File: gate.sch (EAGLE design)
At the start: 42 parts, among them IC1 MAX3232CSE, IC2 LM386M-1, IC3 STM32F072XX, J1 RJ11-2X, X1 MINI-USB-SCHIELD-32005-301

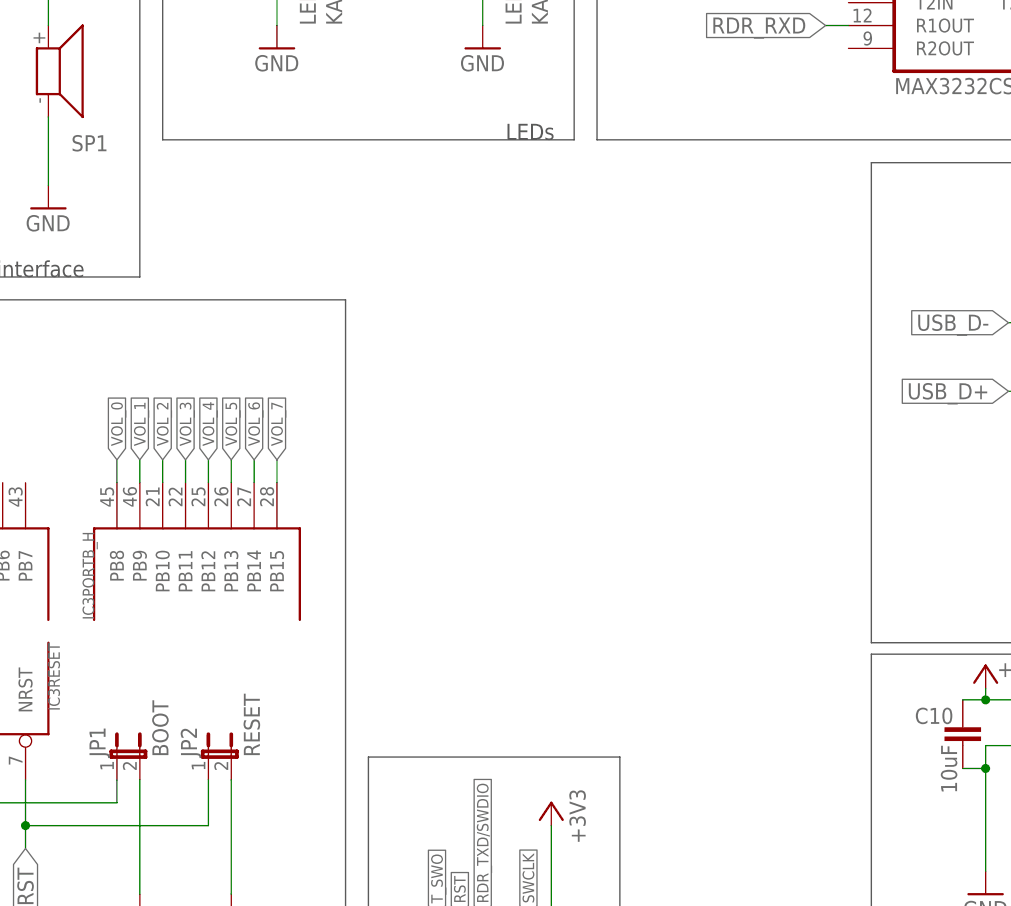
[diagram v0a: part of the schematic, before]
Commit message: Add power supply
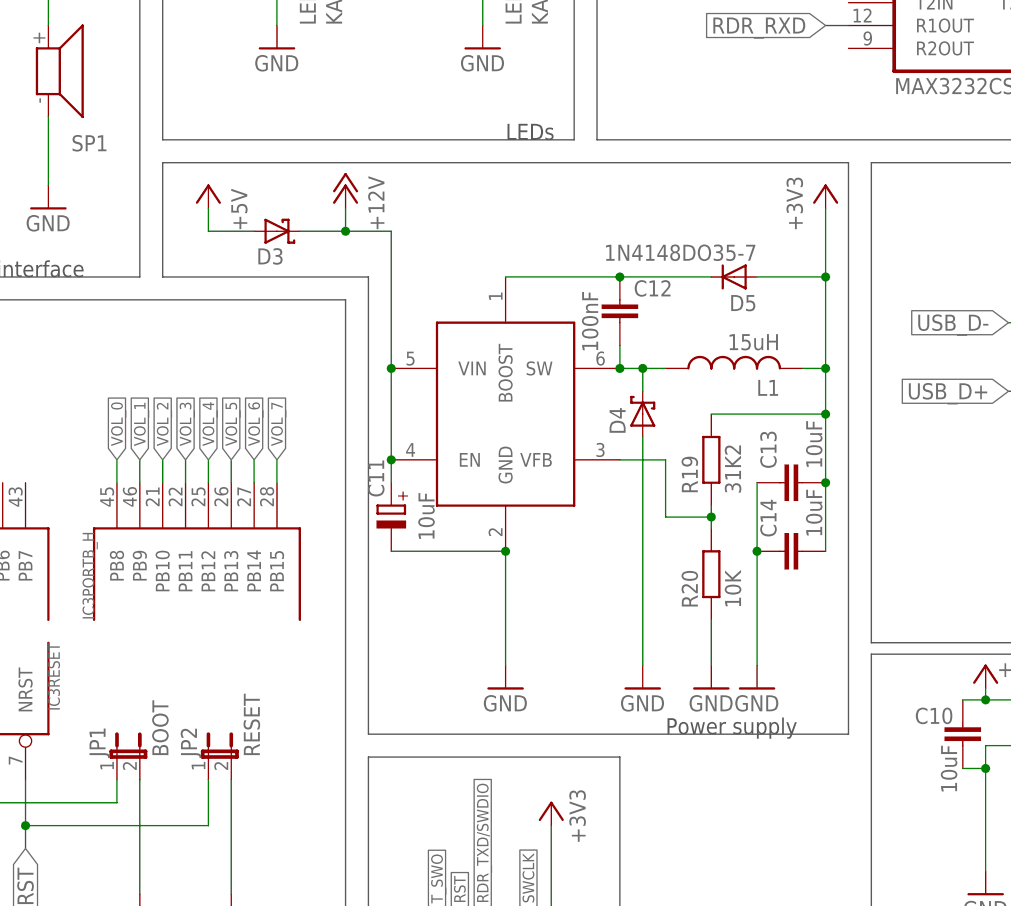
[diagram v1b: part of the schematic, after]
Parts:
- added C11: 10uF, rcl:CPOL-EU153CLV-0505
- added C12: 100nF, rcl:C-EUC0805
- added C13, C14: 10uF, rcl:C-EUC0805
- added D3, D4: (no value), diode:SCHOTTKY-DIODESMD
- added D5: 1N4148DO35-7, diode:1N4148DO35-7
- added L1: 15uH, rcl:L-USPIS2816
- added R19: 31K2, rcl:R-EU_R0805
- added R20: 10K, rcl:R-EU_R0805
- added U$1: MCP16301/H, MCP16301:MCP16301/H
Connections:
- new net N$22: C12.2, D4.C, L1.1, U$1.SW
- new net N$23: C12.1, D5.C, U$1.BOOST
- new net N$25: R19.1, R20.2, U$1.VFB
- net +12V: now also C11.+, D3.C, U$1.EN, U$1.VIN
- net +3V3: now also C13.2, C14.2, D5.A, L1.2, R19.2
- net +5V: now also D3.A
- net GND: now also C11.-, C13.1, C14.1, D4.A, R20.1, U$1.GND
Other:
- note added: "Power supply"
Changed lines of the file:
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@@
 <part name="+3V6" library="supply1" deviceset="+3V3" device=""/>
 <part name="GND16" library="supply1" deviceset="GND" device=""/>
+<part name="U$1" library="MCP16301" deviceset="MCP16301/H" device=""/>
+<part name="P+4" library="supply1" deviceset="+5V" device=""/>
+<part name="P+5" library="supply1" deviceset="+12V" device=""/>
+<part name="D3" library="diode" deviceset="SCHOTTKY-DIODE" device="SMD"/>
+<part name="C11" library="rcl" deviceset="CPOL-EU" device="153CLV-0505" value="10uF"/>
+<part name="GND17" library="supply1" deviceset="GND" device=""/>
+<part name="C12" library="rcl" deviceset="C-EU" device="C0805" value="100nF"/>
+<part name="D4" library="diode" deviceset="SCHOTTKY-DIODE" device="SMD"/>
+<part name="GND18" library="supply1" deviceset="GND" device=""/>
+<part name="L1" library="rcl" deviceset="L-US" device="PIS2816" value="15uH"/>
+<part name="D5" library="diode" deviceset="1N4148" device="DO35-7"/>
+<part name="R19" library="rcl" deviceset="R-EU_" device="R0805" value="31K2"/>
+<part name="R20" library="rcl" deviceset="R-EU_" device="R0805" value="10K"/>
+<part name="GND19" library="supply1" deviceset="GND" device=""/>
+<part name="+3V7" library="supply1" deviceset="+3V3" device=""/>
+<part name="C13" library="rcl" deviceset="C-EU" device="C0805" value="10uF"/>
+<part name="C14" library="rcl" deviceset="C-EU" device="C0805" value="10uF"/>
+<part name="GND20" library="supply1" deviceset="GND" device=""/>
 </parts>
 <sheets>
@@
 <wire x1="129.54" y1="10.16" x2="129.54" y2="45.72" width="0.1524" layer="97"/>
 <text x="152.4" y="10.16" size="1.778" layer="97">SWD</text>
+<wire x1="106.68" y1="111.76" x2="182.88" y2="111.76" width="0.1524" layer="97"/>
+<wire x1="182.88" y1="111.76" x2="182.88" y2="48.26" width="0.1524" layer="97"/>
+<wire x1="182.88" y1="48.26" x2="129.54" y2="48.26" width="0.1524" layer="97"/>
+<wire x1="129.54" y1="48.26" x2="129.54" y2="99.06" width="0.1524" layer="97"/>
+<wire x1="129.54" y1="99.06" x2="106.68" y2="99.06" width="0.1524" layer="97"/>
+<wire x1="106.68" y1="99.06" x2="106.68" y2="111.76" width="0.1524" layer="97"/>
+<text x="162.56" y="48.26" size="1.778" layer="97">Power supply</text>
 </plain>
 <instances>
@@
 </instance>
 <instance part="GND16" gate="1" x="144.78" y="15.24"/>
+<instance part="U$1" gate="G$1" x="144.78" y="83.82"/>
+<instance part="P+4" gate="1" x="111.76" y="109.22" rot="MR0"/>
+<instance part="P+5" gate="1" x="127" y="109.22" rot="MR0"/>
+<instance part="D3" gate="G$1" x="119.38" y="104.14" rot="MR180"/>
+<instance part="C11" gate="G$1" x="132.08" y="73.66" smashed="yes" rot="MR0">
+<attribute name="NAME" x="129.5146" y="74.549" size="1.778" layer="95" rot="MR90"/>
+<attribute name="VALUE" x="135.1026" y="69.723" size="1.778" layer="96" rot="MR90"/>
+</instance>
+<instance part="GND17" gate="1" x="144.78" y="53.34"/>
+<instance part="C12" gate="G$1" x="157.48" y="96.52" smashed="yes">
+<attribute name="NAME" x="159.004" y="96.901" size="1.778" layer="95"/>
+<attribute name="VALUE" x="155.067" y="90.678" size="1.778" layer="96" rot="R90"/>
+</instance>
+<instance part="D4" gate="G$1" x="160.02" y="83.82" rot="R90"/>
+<instance part="GND18" gate="1" x="160.02" y="53.34"/>
+<instance part="L1" gate="G$1" x="170.18" y="88.9" rot="R90"/>
+<instance part="D5" gate="G$1" x="170.18" y="99.06" smashed="yes" rot="R180">
+<attribute name="NAME" x="172.72" y="97.0534" size="1.778" layer="95" rot="R180"/>
+<attribute name="VALUE" x="172.72" y="102.6414" size="1.778" layer="96" rot="R180"/>
+</instance>
+<instance part="R19" gate="G$1" x="167.64" y="78.74" rot="R90"/>
+<instance part="R20" gate="G$1" x="167.64" y="66.04" rot="R90"/>
+<instance part="GND19" gate="1" x="167.64" y="53.34"/>
+<instance part="+3V7" gate="G$1" x="180.34" y="109.22"/>
+<instance part="C13" gate="G$1" x="175.26" y="76.2" rot="R90"/>
+<instance part="C14" gate="G$1" x="175.26" y="68.58" rot="R90"/>
+<instance part="GND20" gate="1" x="172.72" y="53.34"/>
 </instances>
 <busses>
@@
 <wire x1="144.78" y1="22.86" x2="144.78" y2="17.78" width="0.1524" layer="91"/>
 </segment>
+<segment>
+<pinref part="C11" gate="G$1" pin="-"/>
+<pinref part="U$1" gate="G$1" pin="GND"/>
+<wire x1="132.08" y1="68.58" x2="144.78" y2="68.58" width="0.1524" layer="91"/>
+<pinref part="GND17" gate="1" pin="GND"/>
+<wire x1="144.78" y1="68.58" x2="144.78" y2="55.88" width="0.1524" layer="91"/>
+<junction x="144.78" y="68.58"/>
+</segment>
+<segment>
+<pinref part="D4" gate="G$1" pin="A"/>
+<pinref part="GND18" gate="1" pin="GND"/>
+<wire x1="160.02" y1="81.28" x2="160.02" y2="55.88" width="0.1524" layer="91"/>
+</segment>
+<segment>
+<pinref part="R20" gate="G$1" pin="1"/>
+<pinref part="GND19" gate="1" pin="GND"/>
+<wire x1="167.64" y1="60.96" x2="167.64" y2="55.88" width="0.1524" layer="91"/>
+</segment>
+<segment>
+<pinref part="C13" gate="G$1" pin="1"/>
+<pinref part="C14" gate="G$1" pin="1"/>
+<wire x1="172.72" y1="76.2" x2="172.72" y2="68.58" width="0.1524" layer="91"/>
+<pinref part="GND20" gate="1" pin="GND"/>
+<wire x1="172.72" y1="68.58" x2="172.72" y2="55.88" width="0.1524" layer="91"/>
+<junction x="172.72" y="68.58"/>
+</segment>
 </net>
 <net name="N$1" class="0">
@@
 <wire x1="149.86" y1="38.1" x2="149.86" y2="22.86" width="0.1524" layer="91"/>
 </segment>
+<segment>
+<pinref part="D5" gate="G$1" pin="A"/>
+<wire x1="180.34" y1="99.06" x2="172.72" y2="99.06" width="0.1524" layer="91"/>
+<wire x1="180.34" y1="99.06" x2="180.34" y2="106.68" width="0.1524" layer="91"/>
+<pinref part="+3V7" gate="G$1" pin="+3V3"/>
+<pinref part="R19" gate="G$1" pin="2"/>
+<wire x1="167.64" y1="83.82" x2="180.34" y2="83.82" width="0.1524" layer="91"/>
+<wire x1="180.34" y1="99.06" x2="180.34" y2="88.9" width="0.1524" layer="91"/>
+<junction x="180.34" y="99.06"/>
+<pinref part="L1" gate="G$1" pin="2"/>
+<wire x1="180.34" y1="88.9" x2="180.34" y2="83.82" width="0.1524" layer="91"/>
+<wire x1="177.8" y1="88.9" x2="180.34" y2="88.9" width="0.1524" layer="91"/>
+<junction x="180.34" y="88.9"/>
+<pinref part="C13" gate="G$1" pin="2"/>
+<wire x1="180.34" y1="83.82" x2="180.34" y2="76.2" width="0.1524" layer="91"/>
+<junction x="180.34" y="83.82"/>
+<pinref part="C14" gate="G$1" pin="2"/>
+<wire x1="180.34" y1="76.2" x2="180.34" y2="68.58" width="0.1524" layer="91"/>
+<junction x="180.34" y="76.2"/>
+</segment>
 </net>
 <net name="N$3" class="0">
@@
 <pinref part="IC2" gate="G$1" pin="VS"/>
 <wire x1="58.42" y1="147.32" x2="58.42" y2="142.24" width="0.1524" layer="91"/>
+</segment>
+<segment>
+<pinref part="P+4" gate="1" pin="+5V"/>
+<wire x1="111.76" y1="104.14" x2="111.76" y2="106.68" width="0.1524" layer="91"/>
+<pinref part="D3" gate="G$1" pin="A"/>
+<wire x1="116.84" y1="104.14" x2="111.76" y2="104.14" width="0.1524" layer="91"/>
 </segment>
 </net>
@@
 <pinref part="P+1" gate="1" pin="+12V"/>
 </segment>
+<segment>
+<pinref part="D3" gate="G$1" pin="C"/>
+<pinref part="P+5" gate="1" pin="+12V"/>
+<wire x1="127" y1="106.68" x2="127" y2="104.14" width="0.1524" layer="91"/>
+<wire x1="127" y1="104.14" x2="121.92" y2="104.14" width="0.1524" layer="91"/>
+<pinref part="U$1" gate="G$1" pin="VIN"/>
+<wire x1="132.08" y1="88.9" x2="132.08" y2="78.74" width="0.1524" layer="91"/>
+<pinref part="U$1" gate="G$1" pin="EN"/>
+<pinref part="C11" gate="G$1" pin="+"/>
+<wire x1="132.08" y1="78.74" x2="132.08" y2="76.2" width="0.1524" layer="91"/>
+<junction x="132.08" y="78.74"/>
+<junction x="132.08" y="88.9"/>
+<wire x1="127" y1="104.14" x2="132.08" y2="104.14" width="0.1524" layer="91"/>
+<wire x1="132.08" y1="104.14" x2="132.08" y2="88.9" width="0.1524" layer="91"/>
+<junction x="127" y="104.14"/>
+</segment>
 </net>
 <net name="N$19" class="0">
@@
 </segment>
 </net>
+<net name="N$22" class="0">
+<segment>
+<pinref part="U$1" gate="G$1" pin="SW"/>
+<pinref part="C12" gate="G$1" pin="2"/>
+<wire x1="157.48" y1="88.9" x2="157.48" y2="91.44" width="0.1524" layer="91"/>
+<pinref part="D4" gate="G$1" pin="C"/>
+<wire x1="157.48" y1="88.9" x2="160.02" y2="88.9" width="0.1524" layer="91"/>
+<wire x1="160.02" y1="88.9" x2="160.02" y2="86.36" width="0.1524" layer="91"/>
+<junction x="157.48" y="88.9"/>
+<pinref part="L1" gate="G$1" pin="1"/>
+<wire x1="162.56" y1="88.9" x2="160.02" y2="88.9" width="0.1524" layer="91"/>
+<junction x="160.02" y="88.9"/>
+</segment>
+</net>
+<net name="N$23" class="0">
+<segment>
+<pinref part="C12" gate="G$1" pin="1"/>
+<pinref part="U$1" gate="G$1" pin="BOOST"/>
+<wire x1="157.48" y1="99.06" x2="144.78" y2="99.06" width="0.1524" layer="91"/>
+<pinref part="D5" gate="G$1" pin="C"/>
+<wire x1="167.64" y1="99.06" x2="157.48" y2="99.06" width="0.1524" layer="91"/>
+<junction x="157.48" y="99.06"/>
+</segment>
+</net>
+<net name="N$25" class="0">
+<segment>
+<pinref part="R19" gate="G$1" pin="1"/>
+<pinref part="R20" gate="G$1" pin="2"/>
+<wire x1="167.64" y1="73.66" x2="167.64" y2="72.39" width="0.1524" layer="91"/>
+<wire x1="167.64" y1="72.39" x2="167.64" y2="71.12" width="0.1524" layer="91"/>
+<wire x1="167.64" y1="72.39" x2="162.56" y2="72.39" width="0.1524" layer="91"/>
+<wire x1="162.56" y1="72.39" x2="162.56" y2="78.74" width="0.1524" layer="91"/>
+<junction x="167.64" y="72.39"/>
+<pinref part="U$1" gate="G$1" pin="VFB"/>
+<wire x1="162.56" y1="78.74" x2="157.48" y2="78.74" width="0.1524" layer="91"/>
+</segment>
+</net>

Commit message: Finishing touches for revA
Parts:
- removed U$1: MCP16301/H, MCP16301:MCP16301/H
- added IC4: MAX3232CSE, maxim:MAX3232CSE
- added R21: 100K, rcl:R-EU_R0805
- C1, C2, C3: value (none) -> 10uF; device rcl:CPOL-EU153CLV-0505 -> rcl:C-EUC0805
- C10, C13, C14: value 10uF -> (none); device rcl:C-EUC0805 -> rcl:CPOL-EU153CLV-0505
- C11: value 10uF -> (none)
- C12: value 100nF -> 10uF
- C4: value (none) -> 50nF; device rcl:CPOL-EU153CLV-0505 -> rcl:C-EUC0805
- C5: value 50nF -> 250uF
- C6: value 250uF -> 10uF; device rcl:C-EUC0805 -> rcl:CPOL-EU153CLV-0505
- C7: value 10uF -> 100nF
- D3: value (none) -> 1N4148DO35-7; device diode:SCHOTTKY-DIODESMD -> diode:1N4148DO35-7
- D5: value 1N4148DO35-7 -> (none); device diode:1N4148DO35-7 -> diode:SCHOTTKY-DIODESMD
- IC1: value MAX3232CSE -> LM386M-1; device maxim:MAX3232CSE -> linear:LM386M-1
- IC2: value LM386M-1 -> STM32F072XX; device linear:LM386M-1 -> stm32f051:STM32F072XX
- IC3: value STM32F072XX -> MCP16301/H; device stm32f051:STM32F072XX -> MCP16301:MCP16301/H
- R1, R2: value 22R -> TODO
- R10, R7, R8, R9: value 330R -> TODO
- R11: value TODO -> 10R
- R12, R13, R14, R15: value TODO -> 330R
- R16: value TODO -> 31K2
- R17: value TODO -> 10K
- R18: value TODO -> 22R
- R19: value 31K2 -> 22R
- R20: value 10K -> 1K5
- R3: value 100K -> TODO
- R4: value 1K5 -> TODO
- R6: value 10R -> TODO
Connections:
- net +12V: now also C6.+, D5.C, IC3.EN, IC3.VIN; no longer C11.+, D3.C, U$1.EN, U$1.VIN
- net +3V3: now also C1.1, C12.1, C13.-, C2.1, C3.1, C8.2, C9.2, D3.A, IC2AN_POWER.VBAT, IC2AN_POWER.VDDA, IC2POWER.VDD_1, IC2POWER.VDD_2, IC2POWER.VDD_3, IC4P.VCC, R16.2, R20.1; no longer C1.-, C10.1, C13.2, C14.2, C7.1, C8.1, C9.1, D5.A, IC1P.VCC, IC3AN_POWER.VBAT, IC3AN_POWER.VDDA, IC3POWER.VDD_1, IC3POWER.VDD_2, IC3POWER.VDD_3, R19.2, R4.1
- net +5V: now also D1.A, D4.C, IC1.VS; no longer D2.C, D3.A, IC2.VS
- net AUDIO_OUT: now also IC2PORTA_L.PA4, R10.2; no longer IC3PORTA_L.PA4, R5.2
- net BOOT0: now also IC2RESET.BOOT0; no longer IC3RESET.BOOT0
- net GND: now also C1.2, C12.2, C14.+, C2.2, C3.2, C6.-, C8.1, C9.1, D2.A, IC1.-IN, IC1.GND, IC2AN_POWER.VSSA, IC2POWER.VSS_1, IC2POWER.VSS_2, IC2POWER.VSS_3, IC3.GND, IC4P.GND, R11.1, R17.1, R21.1, R9.1; no longer C10.2, C11.-, C13.1, C14.1, C2.+, C7.2, C8.2, C9.2, D4.A, IC1P.GND, IC2.-IN, IC2.GND, IC3AN_POWER.VSSA, IC3POWER.VSS_1, IC3POWER.VSS_2, IC3POWER.VSS_3, R20.1, R3.1, R6.1, U$1.GND
- net LED_G1: now also IC2PORTB_L.PB1, R13.2; no longer IC3PORTB_L.PB1, R8.2
- net LED_G2: now also IC2PORTA_H.PA8, R15.2; no longer IC3PORTA_H.PA8, R10.2
- net LED_R1: now also IC2PORTB_L.PB0, R12.2; no longer IC3PORTB_L.PB0, R7.2
- net LED_R2: now also IC2PORTA_H.PA9, R14.2; no longer IC3PORTA_H.PA9, R9.2
- net N$1: now also IC4G$1.R1IN; no longer IC1G$1.R1IN
- net N$10: now also R14.1; no longer R9.1
- net N$11: now also D4.A; no longer D2.A
- net N$12: now also R18.2; no longer R1.2
- net N$13: now also R19.2, R20.2; no longer R2.2, R4.2
- net N$14: now also R21.2; no longer R3.2
- net N$15: now also IC1.+IN, R1.2, R10.1, R2.2, R3.2, R4.2, R5.2, R6.2, R7.2, R8.2, R9.2; no longer IC2.+IN, R11.2, R12.2, R13.2, R14.2, R15.2, R16.2, R17.2, R18.2, R5.1
- net N$16: now also C4.1, IC1.OUT; no longer C6.1, IC2.OUT
- net N$17: now also C4.2, R11.2; no longer C5.2, R6.2
- net N$18: now also C5.2; no longer C6.2
- net N$19: now also R12.1; no longer R7.1
- net N$2: now also IC4G$1.T1OUT; no longer IC1G$1.T1OUT
- net N$20: now also R13.1; no longer R8.1
- net N$21: now also R15.1; no longer R10.1
- net N$22: now also C7.2, D2.C, IC3.SW; no longer C12.2, D4.C, U$1.SW
- net N$23: now also C7.1, D3.C, IC3.BOOST; no longer C12.1, D5.C, U$1.BOOST
- net N$25: now also IC3.VFB, R16.1, R17.2; no longer R19.1, R20.2, U$1.VFB
- net N$3: now also C10.+, IC4G$1.C1+; no longer C3.+, IC1G$1.C1+
- net N$4: now also C10.-, IC4G$1.C1-; no longer C3.-, IC1G$1.C1-
- net N$5: now also C11.+, IC4G$1.C2+; no longer C4.+, IC1G$1.C2+
- net N$6: now also C11.-, IC4G$1.C2-; no longer C4.-, IC1G$1.C2-
- net N$7: now also C13.+, IC4G$1.V+; no longer C1.+, IC1G$1.V+
- net N$8: now also C14.-, IC4G$1.V-; no longer C2.-, IC1G$1.V-
- net N$9: now also D5.A; no longer D1.A
- net RDR_RXD: now also IC2PORTA_H.PA15, IC4G$1.R1OUT; no longer IC1G$1.R1OUT, IC3PORTA_H.PA15
- net RDR_TXD/SWDIO: now also IC2PORTA_H.PA14, IC4G$1.T1IN; no longer IC1G$1.T1IN, IC3PORTA_H.PA14
- net RFID_IRQ: now also IC2PORTA_L.PA0; no longer IC3PORTA_L.PA0
- net RFID_MISO: now also IC2PORTA_L.PA6; no longer IC3PORTA_L.PA6
- net RFID_MOSI: now also IC2PORTA_L.PA7; no longer IC3PORTA_L.PA7
- net RFID_RST: now also IC2PORTA_L.PA3; no longer IC3PORTA_L.PA3
- net RFID_SCK: now also IC2PORTA_L.PA5; no longer IC3PORTA_L.PA5
- net RFID_SS: now also IC2PORTA_L.PA1; no longer IC3PORTA_L.PA1
- net RST: now also IC2RESET.NRST; no longer IC3RESET.NRST
- net SWCLK: now also IC2PORTA_H.PA13; no longer IC3PORTA_H.PA13
- net T_SWO: now also IC2PORTB_L.PB3; no longer IC3PORTB_L.PB3
- net USB_D+: now also IC2PORTA_H.PA11, R19.1; no longer IC3PORTA_H.PA11, R2.1
- net USB_D-: now also IC2PORTA_H.PA12, R18.1; no longer IC3PORTA_H.PA12, R1.1
- net VOL_0: now also IC2PORTB_H.PB8, R1.1; no longer IC3PORTB_H.PB8, R11.1
- net VOL_1: now also IC2PORTB_H.PB9, R2.1; no longer IC3PORTB_H.PB9, R12.1
- net VOL_2: now also IC2PORTB_H.PB10, R3.1; no longer IC3PORTB_H.PB10, R13.1
- net VOL_3: now also IC2PORTB_H.PB11, R4.1; no longer IC3PORTB_H.PB11, R14.1
- net VOL_4: now also IC2PORTB_H.PB12, R5.1; no longer IC3PORTB_H.PB12, R15.1
- net VOL_5: now also IC2PORTB_H.PB13, R6.1; no longer IC3PORTB_H.PB13, R16.1
- net VOL_6: now also IC2PORTB_H.PB14, R7.1; no longer IC3PORTB_H.PB14, R17.1
- net VOL_7: now also IC2PORTB_H.PB15, R8.1; no longer IC3PORTB_H.PB15, R18.1
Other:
- note added: "See README.md for component fitting instructions"
- moved on the sheet: C11, C12, C5, C7, C8, C9, D1, D2, D4, R1, R10, R11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

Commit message: Minor value tweaks
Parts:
- removed D5: (no value), diode:SCHOTTKY-DIODESMD
- added R22: 100K, rcl:R-EU_R0805
- C1, C2, C3: value 10uF -> 100nF
- D2: value (none) -> 1N4148DO35-7; device diode:SCHOTTKY-DIODESMD -> diode:1N4148DO35-7
- D3: value 1N4148DO35-7 -> (none); device diode:1N4148DO35-7 -> diode:SCHOTTKY-DIODESMD
- L1: value 15uH -> 22uH
- R12: value 330R -> 510R
- R16: value 31K2 -> 330R
- R17: value 10K -> 31K2
- R18: value 22R -> 10K
- R20: value 1K5 -> 22R
- R21: value 100K -> 1K5
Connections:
- removed net +12V: C6.+, D1.C, D5.C, IC3.EN, IC3.VIN
- removed net +5V: D1.A, D4.C, IC1.VS
- new net V+: C6.+, D3.C, D4.C, IC1.VS, IC3.EN, IC3.VIN
- net +3V3: now also D2.A, R17.2, R21.1; no longer D3.A, R16.2, R20.1
- net BOOT0: now also R12.2
- net GND: now also D1.A, R12.1, R18.1, R22.1; no longer D2.A, R17.1, R21.1
- net LED_G1: now also R14.2; no longer R13.2
- net LED_G2: now also R16.2; no longer R15.2
- net LED_R1: now also R13.2; no longer R12.2
- net LED_R2: now also R15.2; no longer R14.2
- net N$10: now also R15.1; no longer R14.1
- net N$11: now also D3.A; no longer D4.A
- net N$12: now also R19.2; no longer R18.2
- net N$13: now also R21.2; no longer R19.2
- net N$14: now also R22.2; no longer R21.2
- net N$19: now also R13.1; no longer R12.1
- net N$20: now also R14.1; no longer R13.1
- net N$21: now also R16.1; no longer R15.1
- net N$22: now also D1.C; no longer D2.C
- net N$23: now also D2.C; no longer D3.C
- net N$25: now also R17.1, R18.2; no longer R16.1, R17.2
- net N$9: now also D4.A; no longer D5.A
- net USB_D+: now also R20.1; no longer R19.1
- net USB_D-: now also R19.1; no longer R18.1
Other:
- moved on the sheet: D1, D4, R12, R13, R14, R15, R16, R17, R18, R19, R20, R21

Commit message: Review-induced fixes
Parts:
- added D5, D6: (no value), diode:SCHOTTKY-DIODESMD
- added R23: 5K1, rcl:R-EU_R0805
- C6: device rcl:CPOL-EU153CLV-0505 -> rcl:C-EUC3225
- R17: value 31K2 -> 33K
- R22: value 100K -> 1K
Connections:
- removed net N$14: R22.2, X1G$1.4
- new net V_SENSE: D6.A, IC2PORTA_L.PA2, R22.1, R23.2
- net +3V3: now also D5.A, D6.C, JP1.2
- net GND: now also C6.2, R23.1, X1G$1.4; no longer C6.-, JP1.2, R22.1
- net V+: now also C6.1, D5.C, R22.2; no longer C6.+
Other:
- moved on the sheet: R22
